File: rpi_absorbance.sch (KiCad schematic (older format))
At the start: 36 parts, among them CON1 BARREL_JACK, P1 CONN_02X04, P2 CONN_01X02, P3 RPI_HEADER, P4 STEPPER_CONN, P5 CONN_02X04, Q1 ZTX692B, U1 R-78B5.0-1.5L, U2 MUN5216DW1T1G, U3 DRV8825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

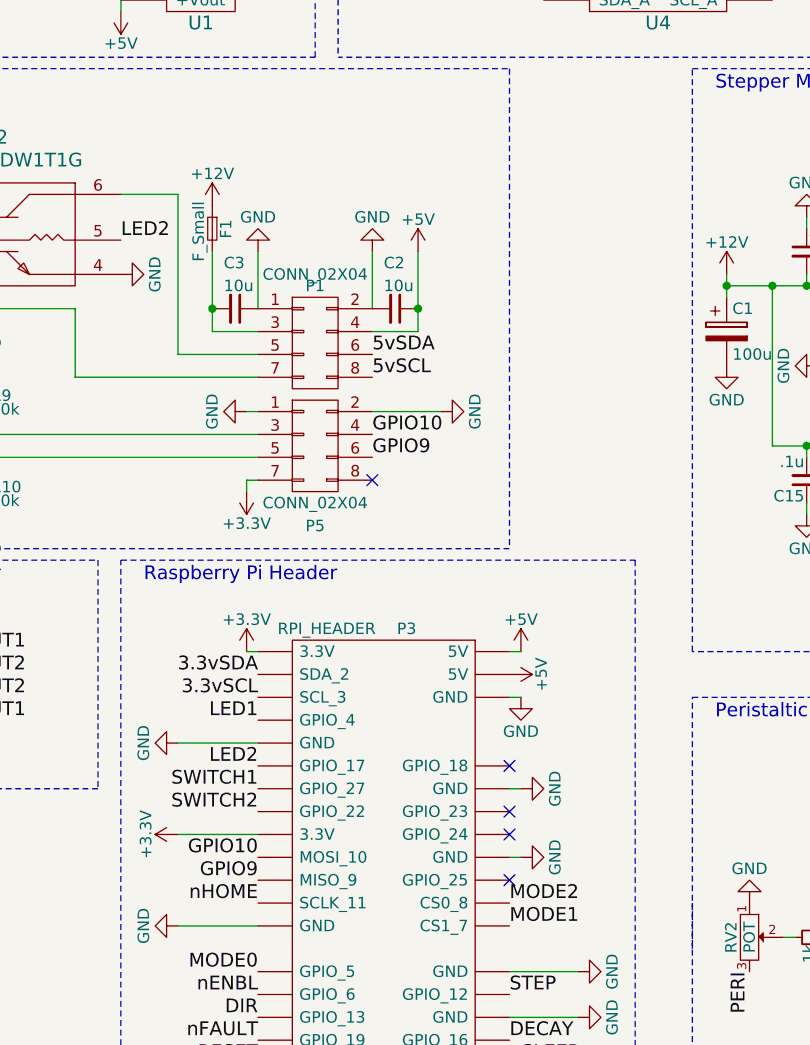
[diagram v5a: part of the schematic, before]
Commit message: Add LED transistor layout
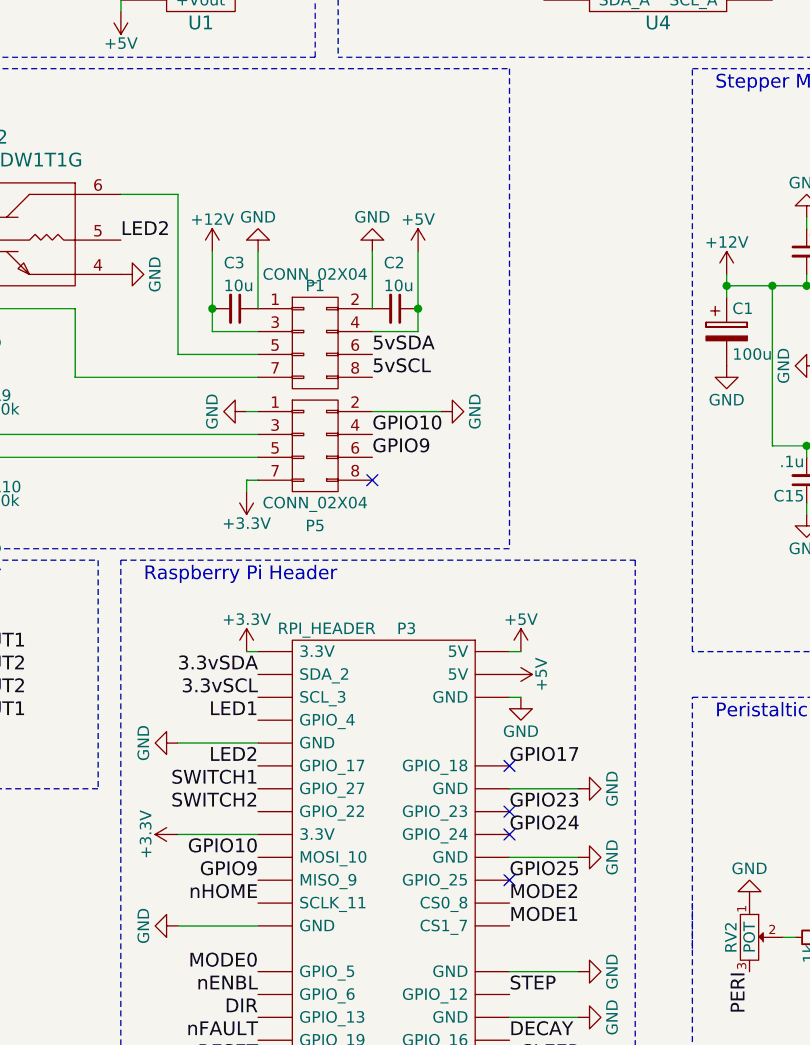
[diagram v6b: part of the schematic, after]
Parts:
- removed F1: F_Small, Discret:CP4, symbol F_Small
- R1: footprint Resistors_SMD:R_0603 -> Resistors_SMD:R_0805_HandSoldering
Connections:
- net +12V: now also C3.2, P1.3 (P3)
- net GPIO17: now reaches P3.12 (GPIO_18)
- net GPIO23: now reaches P3.16 (GPIO_23)
- net GPIO24: now reaches P3.18 (GPIO_24)
- net GPIO25: now reaches P3.22 (GPIO_25)
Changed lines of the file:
@@
 L GND #PWR017
 U 1 1 56CBEAFE
-P 4250 6150
-F 0 "#PWR017" H 4250 5900 50  0001 C CNN
-F 1 "GND" H 4250 6000 50  0000 C CNN
-F 2 "" H 4250 6150 50  0000 C CNN
-F 3 "" H 4250 6150 50  0000 C CNN
-	1    4250 6150
+P 4500 6150
+F 0 "#PWR017" H 4500 5900 50  0001 C CNN
+F 1 "GND" H 4500 6000 50  0000 C CNN
+F 2 "" H 4500 6150 50  0000 C CNN
+F 3 "" H 4500 6150 50  0000 C CNN
+	1    4500 6150
 	0    -1   -1   0
 $EndComp
@@
 L GND #PWR018
 U 1 1 56CBEB42
-P 4250 5850
-F 0 "#PWR018" H 4250 5600 50  0001 C CNN
-F 1 "GND" H 4250 5700 50  0000 C CNN
-F 2 "" H 4250 5850 50  0000 C CNN
-F 3 "" H 4250 5850 50  0000 C CNN
-	1    4250 5850
+P 4500 5850
+F 0 "#PWR018" H 4500 5600 50  0001 C CNN
+F 1 "GND" H 4500 5700 50  0000 C CNN
+F 2 "" H 4500 5850 50  0000 C CNN
+F 3 "" H 4500 5850 50  0000 C CNN
+	1    4500 5850
 	0    -1   -1   0
 $EndComp
@@
 	0    -1   -1   0
 $EndComp
-NoConn ~ 4200 6050
-NoConn ~ 4200 5950
-NoConn ~ 4200 5750
 $Comp
 L PWR_FLAG #FLG022
@@
 F 0 "R1" H 5580 6520 50  0000 L CNN
 F 1 "1k" H 5580 6460 50  0000 L CNN
-F 2 "Resistors_SMD:R_0603" H 5550 6500 50  0001 C CNN
+F 2 "Resistors_SMD:R_0805_HandSoldering" H 5550 6500 50  0001 C CNN
 F 3 "" H 5550 6500 50  0000 C CNN
 	1    5550 6500
@@
 L +12V #PWR046
 U 1 1 56D24636
-P 2900 3300
-F 0 "#PWR046" H 2900 3150 50  0001 C CNN
-F 1 "+12V" H 2900 3440 50  0000 C CNN
-F 2 "" H 2900 3300 50  0000 C CNN
-F 3 "" H 2900 3300 50  0000 C CNN
-	1    2900 3300
+P 2900 3500
+F 0 "#PWR046" H 2900 3350 50  0001 C CNN
+F 1 "+12V" H 2900 3640 50  0000 C CNN
+F 2 "" H 2900 3500 50  0000 C CNN
+F 3 "" H 2900 3500 50  0000 C CNN
+	1    2900 3500
 	1    0    0    -1
 $EndComp
@@
 Text Label 3100 5750 2    60   ~ 0
 LED2
-NoConn ~ 4200 6250
 Text Label 3100 6150 2    60   ~ 0
 GPIO10
@@
 	4200 6650 4500 6650
 Wire Wire Line
-	4200 6150 4250 6150
-Wire Wire Line
-	4200 5850 4250 5850
+	4200 6150 4500 6150
+Wire Wire Line
+	4200 5850 4500 5850
 Wire Wire Line
 	4200 5450 4250 5450
@@
 nHOME
 NoConn ~ 3600 4500
-$Comp
-L F_Small F1
-U 1 1 56D4E462
-P 2900 3400
-F 0 "F1" H 2860 3460 50  0000 L CNN
-F 1 "F_Small" H 2780 3340 50  0000 L CNN
-F 2 "Discret:CP4" H 2900 3400 50  0001 C CNN
-F 3 "" H 2900 3400 50  0000 C CNN
-	1    2900 3400
-	0    1    1    0
-$EndComp
 $Comp
 L CONN_02X04 P1
@@
 	1    0    0    -1
 $EndComp
+Text Label 4200 6250 0    60   ~ 0
+GPIO25
+Text Label 4200 6050 0    60   ~ 0
+GPIO24
+Text Label 4200 5950 0    60   ~ 0
+GPIO23
+Text Label 4200 5750 0    60   ~ 0
+GPIO17
+NoConn ~ 4200 5950
+NoConn ~ 4200 6050
+NoConn ~ 4200 6250
+NoConn ~ 4200 5750
 $EndSCHEMATC

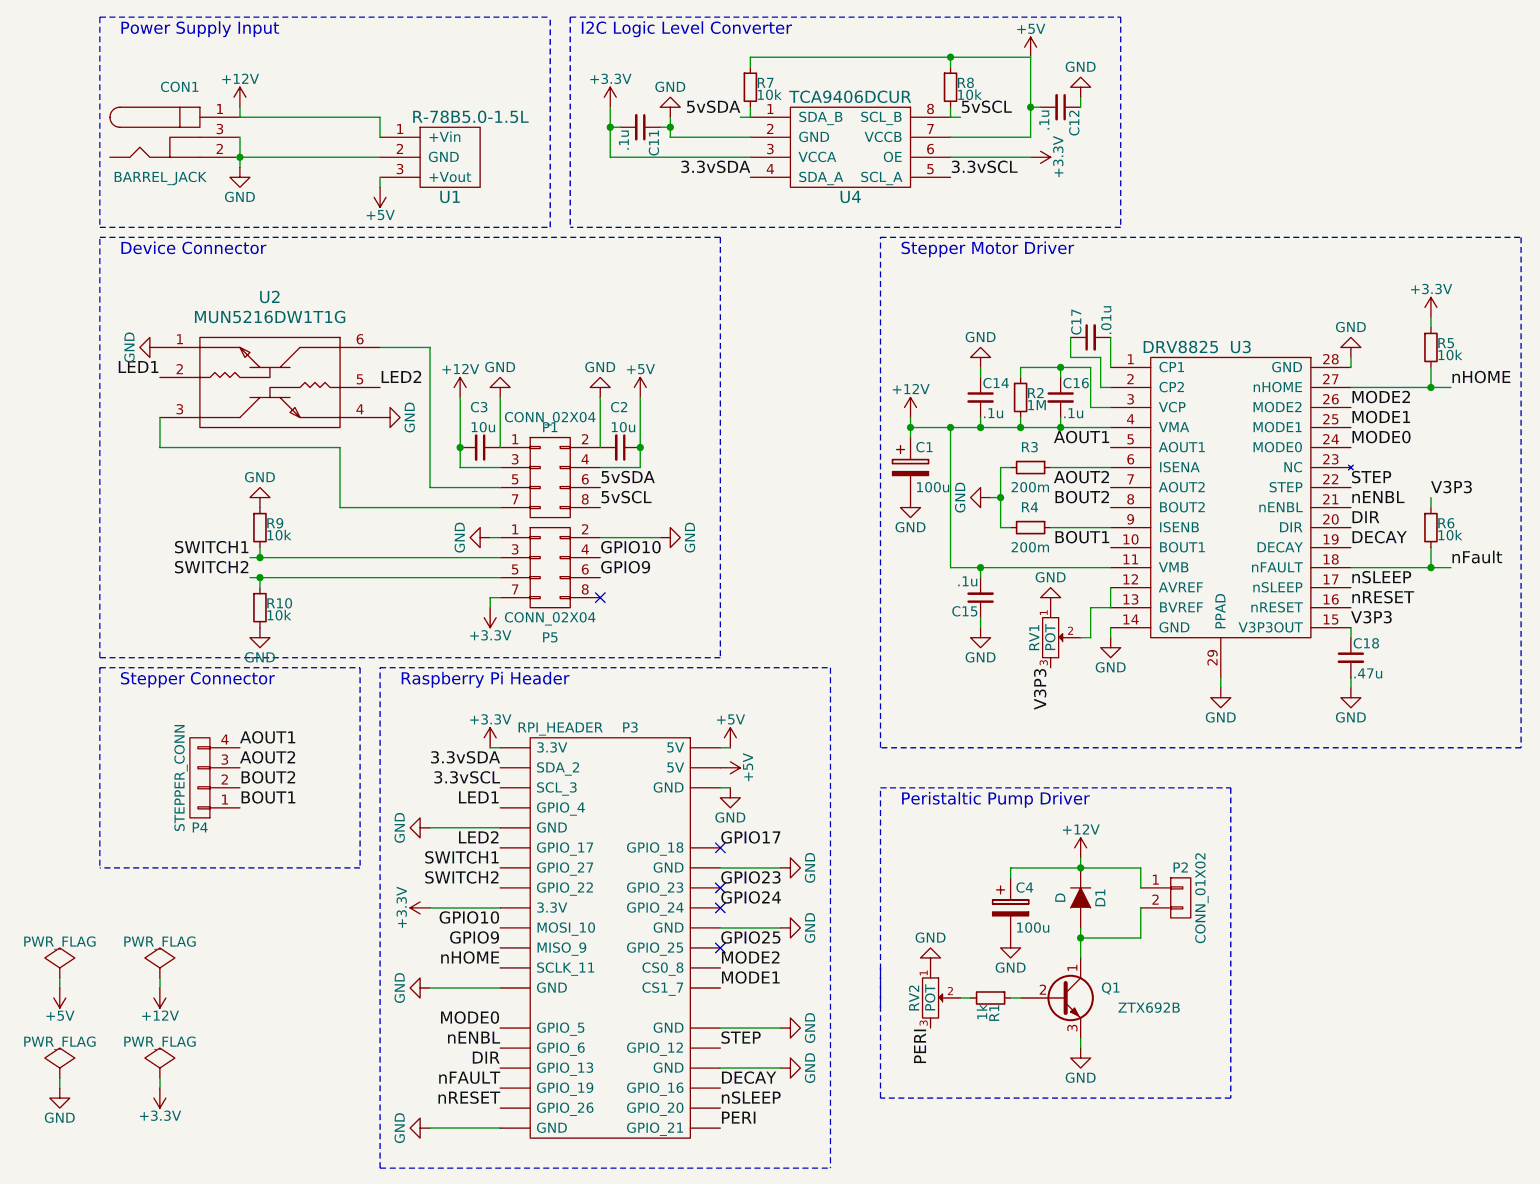
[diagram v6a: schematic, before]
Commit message: Start connecting gpio header
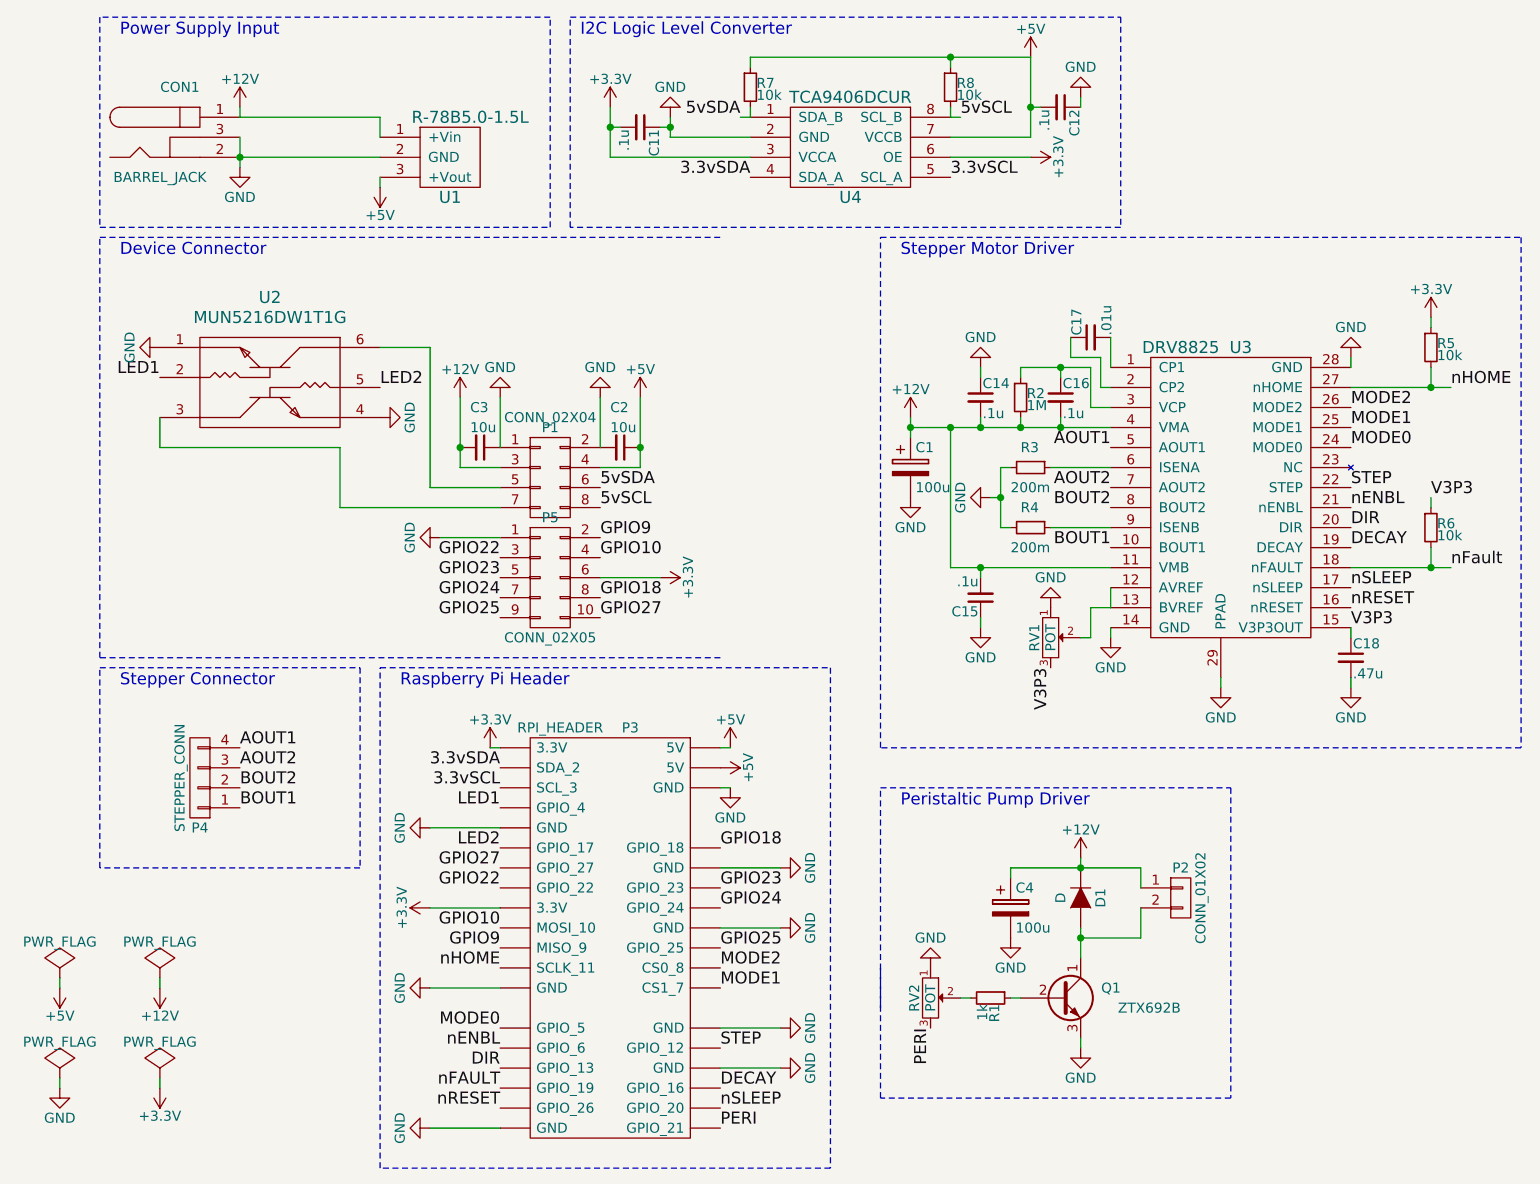
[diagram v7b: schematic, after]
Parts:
- removed P5: CONN_02X04, Pin_Headers:Pin_Header_Straight_2x04, symbol CONN_02X04
- removed R10, R9: 10k, Resistors_SMD:R_0603, symbol R_Small
- added P5: CONN_02X05, Pin_Headers:Pin_Header_Straight_2x05, symbol CONN_02X05
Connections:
- net +3V3: now also P5.6 (P6)
- net GND: now also P5.1 (P1)
- net GPIO10: now also P5.4 (P4)
- net GPIO23: now also P5.5 (P5)
- net GPIO24: now also P5.7 (P7)
- net GPIO25: now also P5.9 (P9)
- net GPIO9: now also P5.2 (P2)
- net GPIO17 renamed GPIO18
- net GPIO18: now also P5.8 (P8)
- net SWITCH1 renamed GPIO27
- net GPIO27: now also P5.10 (P10)
- net SWITCH2 renamed GPIO22
- net GPIO22: now also P5.3 (P3)
- no-connect marks 5 -> 0
